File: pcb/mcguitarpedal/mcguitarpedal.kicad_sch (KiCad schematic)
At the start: 74 parts, among them J1 IN, J10 ENCODER2, J11 ENCODER3, J2 PREAMP_HEADERS, J3 BTN_MTX, J4 OUT, J5 EXP, J6 ILI9488 Module, J7 PWR_IN, J8 POT_HP_VOLUME_10k, J9 ENCODER1, Q1 2N3904, Q2 BC416, SW1 SW_BYPASS, SW2 SW_TUNER, SW3 SW_PRESET, SW5 SW_PWR, U1 Teensy4.1, U2 Teensy Audio Board, U4 74HC148, U6 STPDWN-3P-5V, U7 STDN-3A24-ADJ, U8 74HCT595D

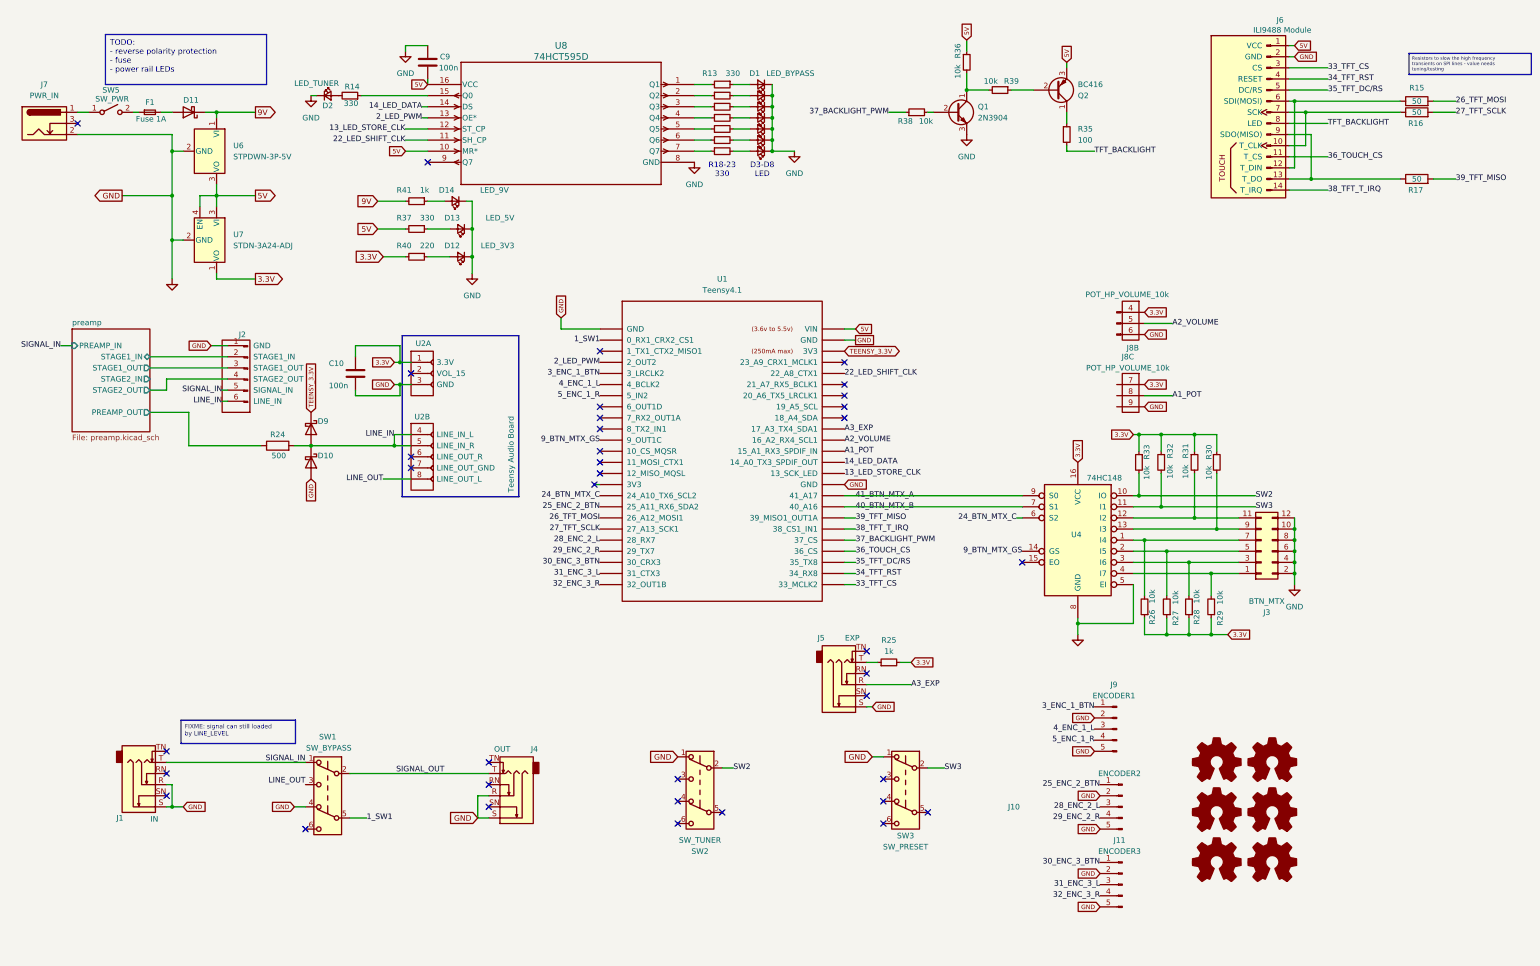
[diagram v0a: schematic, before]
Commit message: Silkscreen labeling
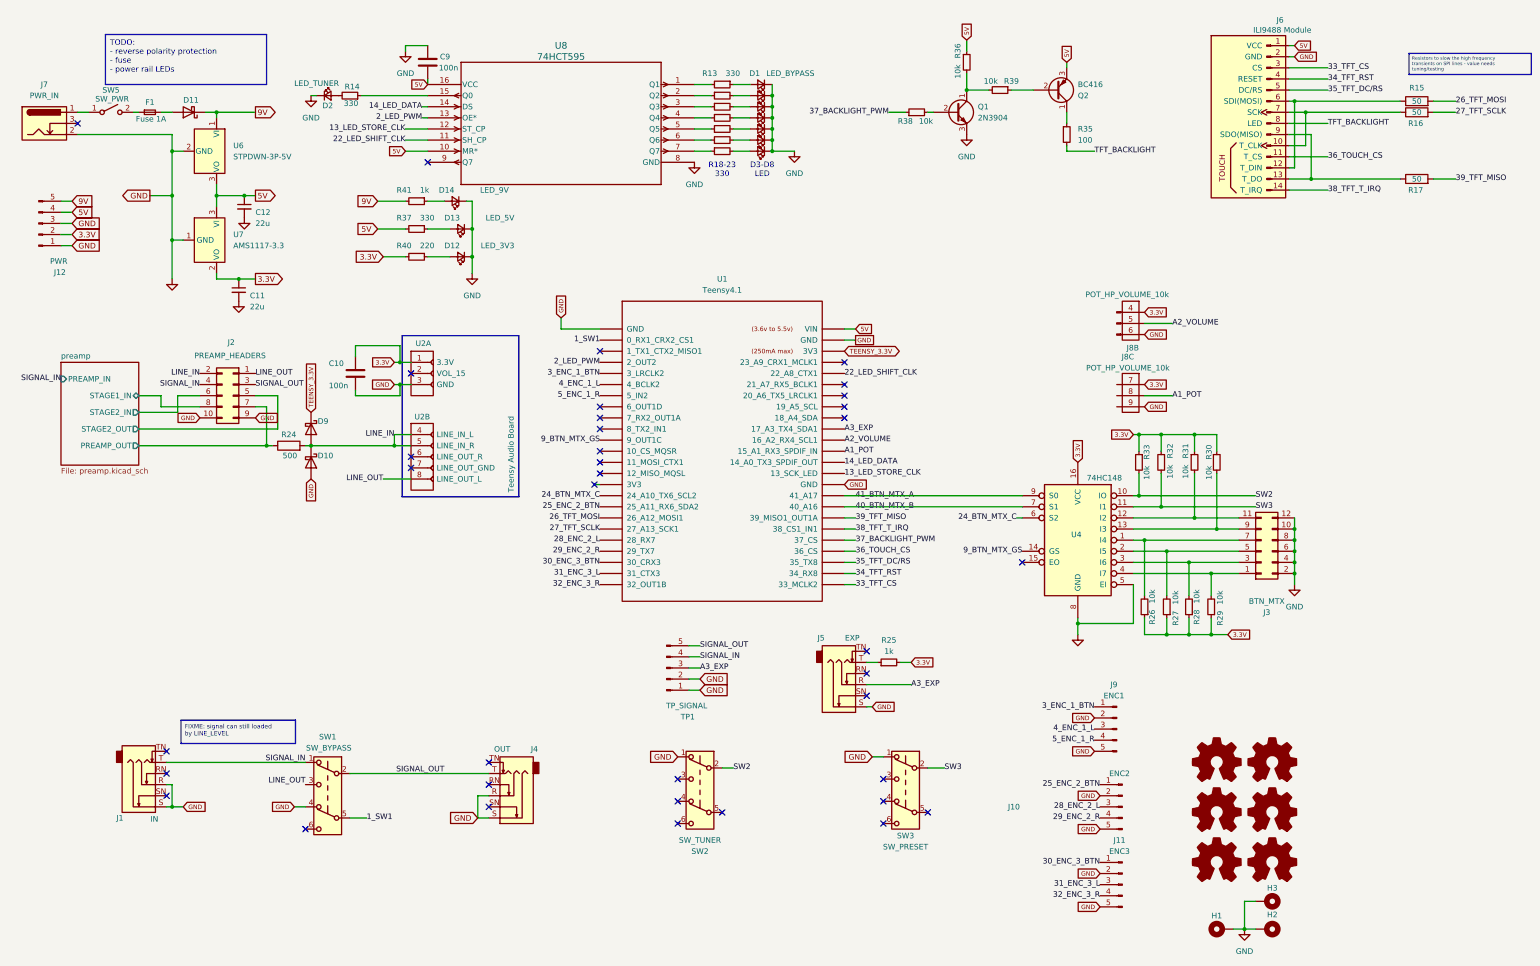
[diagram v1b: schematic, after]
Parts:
- removed U7: STDN-3A24-ADJ, mcguitarpedal:STPDN-3A24-ADJ, symbol mcguitarpedal:STDN-3A24-ADJ
- added C11, C12: 22u, Capacitor_Tantalum_SMD:CP_EIA-7343-30_AVX-N_Pad2.25x2.55mm_HandSolder, symbol Device:C_Small
- added H1, H2, H3: MountingHole_Pad, MountingHole:MountingHole_2.2mm_M2_Pad, symbol Mechanical:MountingHole_Pad
- added J12: PWR, Connector_PinHeader_2.54mm:PinHeader_1x05_P2.54mm_Vertical, symbol Connector:Conn_01x05_Pin
- added TP1: TP_SIGNAL, Connector_PinHeader_2.54mm:PinHeader_1x05_P2.54mm_Vertical, symbol Connector:Conn_01x05_Pin
- added U7: AMS1117-3.3, Package_TO_SOT_SMD:SOT-223-3_TabPin2, symbol Regulator_Linear:AMS1117-3.3
- C9: footprint Capacitor_THT:C_Rect_L7.2mm_W2.5mm_P5.00mm_FKS2_FKP2_MKS2_MKP2 -> Capacitor_SMD:C_1206_3216Metric_Pad1.33x1.80mm_HandSolder
- J10: value ENCODER2 -> ENC2; footprint Connector_PinHeader_2.54mm:PinHeader_1x05_P2.54mm_Vertical -> mcguitarpedal:Encoder_headers
- J11: value ENCODER3 -> ENC3; footprint Connector_PinHeader_2.54mm:PinHeader_1x05_P2.54mm_Vertical -> mcguitarpedal:Encoder_headers
- J2: footprint Connector_PinHeader_2.54mm:PinHeader_1x06_P2.54mm_Vertical -> mcguitarpedal:PREAMP_HEADERS; symbol mcguitarpedal:Preamp_headers -> Connector_Generic:Conn_02x05_Odd_Even
- J9: value ENCODER1 -> ENC1; footprint Connector_PinHeader_2.54mm:PinHeader_1x05_P2.54mm_Vertical -> mcguitarpedal:Encoder_headers
- U8: value 74HCT595D -> 74HCT595
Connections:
- net preamp/STAGE1_OUT is gone; now on net SIGNAL_OUT: J2.3 (Pin_3)
- net 3.3V: now also C11.1, J12.2 (Pin_2), U7.2 (VO)
- net 5V: now also C12.1, J12.4 (Pin_4), U7.3 (VI)
- net 9V: now also J12.5 (Pin_5)
- net A3_EXP: now also TP1.3 (Pin_3)
- net GND: now also J2.10 (Pin_10), J2.9 (Pin_9), C11.2, C12.2, H1.1, H2.1, H3.1, J12.1 (Pin_1), J12.3 (Pin_3), TP1.1 (Pin_1), TP1.2 (Pin_2), U7.1 (GND); no longer J2.1 (GND)
- net LINE_IN: now also J2.2 (Pin_2); no longer J2.6 (LINE_IN)
- net LINE_OUT: now also J2.1 (Pin_1)
- net SIGNAL_IN: now also J2.4 (Pin_4), TP1.4 (Pin_4); no longer J2.5 (SIGNAL_IN)
- net SIGNAL_OUT: now also TP1.5 (Pin_5)
- net preamp/PREAMP_OUT: now also J2.7 (Pin_7)
- net preamp/STAGE1_IN: now also J2.8 (Pin_8); no longer J2.2 (STAGE1_IN)
- net preamp/STAGE2_IN: now also J2.6 (Pin_6)
- net preamp/STAGE2_OUT: now also J2.5 (Pin_5); no longer J2.4 (STAGE2_OUT)
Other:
- sheet preamp ports: added none; removed STAGE1_OUT
- moved on the sheet: R24

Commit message: Final 1.0 design
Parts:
- added C1, C6: 22u, Capacitor_Tantalum_SMD:CP_EIA-3216-18_Kemet-A_Pad1.58x1.35mm_HandSolder, symbol Device:C_Small
- added C2, C4, C9: 100n, Capacitor_SMD:C_1206_3216Metric_Pad1.33x1.80mm_HandSolder, symbol Device:C_Small
- added H1: MountingHole_Pad, MountingHole:MountingHole_2.2mm_M2_Pad, symbol Mechanical:MountingHole_Pad
- added R20: 10k, Resistor_SMD:R_1206_3216Metric_Pad1.30x1.75mm_HandSolder, symbol Device:R_Small
- added TP2: SHIFT_CLK, TestPoint:TestPoint_Loop_D1.80mm_Drill1.0mm_Beaded, symbol Connector:TestPoint
- added TP3: TP_LED_DATA, TestPoint:TestPoint_Loop_D1.80mm_Drill1.0mm_Beaded, symbol Connector:TestPoint
- added TP4: TP_STORE_CLK, TestPoint:TestPoint_Loop_D1.80mm_Drill1.0mm_Beaded, symbol Connector:TestPoint
- added TP5: TP_MOSI, TestPoint:TestPoint_Loop_D1.80mm_Drill1.0mm_Beaded, symbol Connector:TestPoint
- added TP6: TP_SCLK, TestPoint:TestPoint_Loop_D1.80mm_Drill1.0mm_Beaded, symbol Connector:TestPoint
- added TP7: TP_MISO, TestPoint:TestPoint_Loop_D1.80mm_Drill1.0mm_Beaded, symbol Connector:TestPoint
- C3: renamed from C11; footprint Capacitor_Tantalum_SMD:CP_EIA-7343-30_AVX-N_Pad2.25x2.55mm_HandSolder -> Capacitor_Tantalum_SMD:CP_EIA-3216-18_Kemet-A_Pad1.58x1.35mm_HandSolder
- C5: renamed from C12; footprint Capacitor_Tantalum_SMD:CP_EIA-7343-30_AVX-N_Pad2.25x2.55mm_HandSolder -> Capacitor_Tantalum_SMD:CP_EIA-3216-18_Kemet-A_Pad1.58x1.35mm_HandSolder
- C7: renamed from C10; symbol Device:C -> Device:C_Small
- R16: renamed from R25; value 1k -> 330; footprint Resistor_THT:R_Axial_DIN0207_L6.3mm_D2.5mm_P7.62mm_Horizontal -> Resistor_SMD:R_1206_3216Metric_Pad1.30x1.75mm_HandSolder
- renumbered C9 to C8, D11 to D1, D7 to D10, D6 to D11, D5 to D12, D4 to D13, D3 to D14, D9 to D2, D10 to D3, D2 to D4, D14 to D5, D13 to D6, D12 to D7, D1 to D8, D8 to D9, H1 to H2, H2 to H4, J4 to J1, J3 to J12, J5 to J2, J1 to J3, J12 to J4, J7 to J5, J2 to J6, J6 to J7, R24 to R1, R20 to R10, R19 to R11, R18 to R12, R38 to R13, R36 to R14, R39 to R15, R35 to R17, R33 to R18, R26 to R19, R14 to R2, R32 to R21, R27 to R22, R28 to R23, R31 to R24, R29 to R25, R30 to R26, R15 to R27, R16 to R28, R17 to R29, R41 to R3, R37 to R4, R40 to R5, R13 to R6, R23 to R7, R22 to R8, R21 to R9, SW5 to SW1, SW1 to SW2, SW2 to SW3, SW3 to SW4, U6 to U4, U7 to U5, U8 to U6, U4 to U7
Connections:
- net 13_LED_STORE_CLK: now also TP4.1
- net 14_LED_DATA: now also TP3.1
- net 22_LED_SHIFT_CLK: now also TP2.1
- net 3.3V: now also C6.1, C9.1, R20.2
- net 36_TOUCH_CS: now also R20.1
- net 39_TFT_MISO: now also TP7.1
- net 5V: now also C1.2, C2.1
- net 9V: now also C4.1
- net GND: now also C1.1, C2.2, C4.2, C6.2, C9.2, H1.1
- net at J7.12 (T_DIN), J7.6 (SDI(MOSI)), R27.1: now also TP5.1
- net at J7.10 (T_CLK), J7.7 (SCK), R28.1: now also TP6.1
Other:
- moved on the sheet: C3, D5, D6, D7, J7, Q1, Q2, R13, R14, R15, R17, R27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

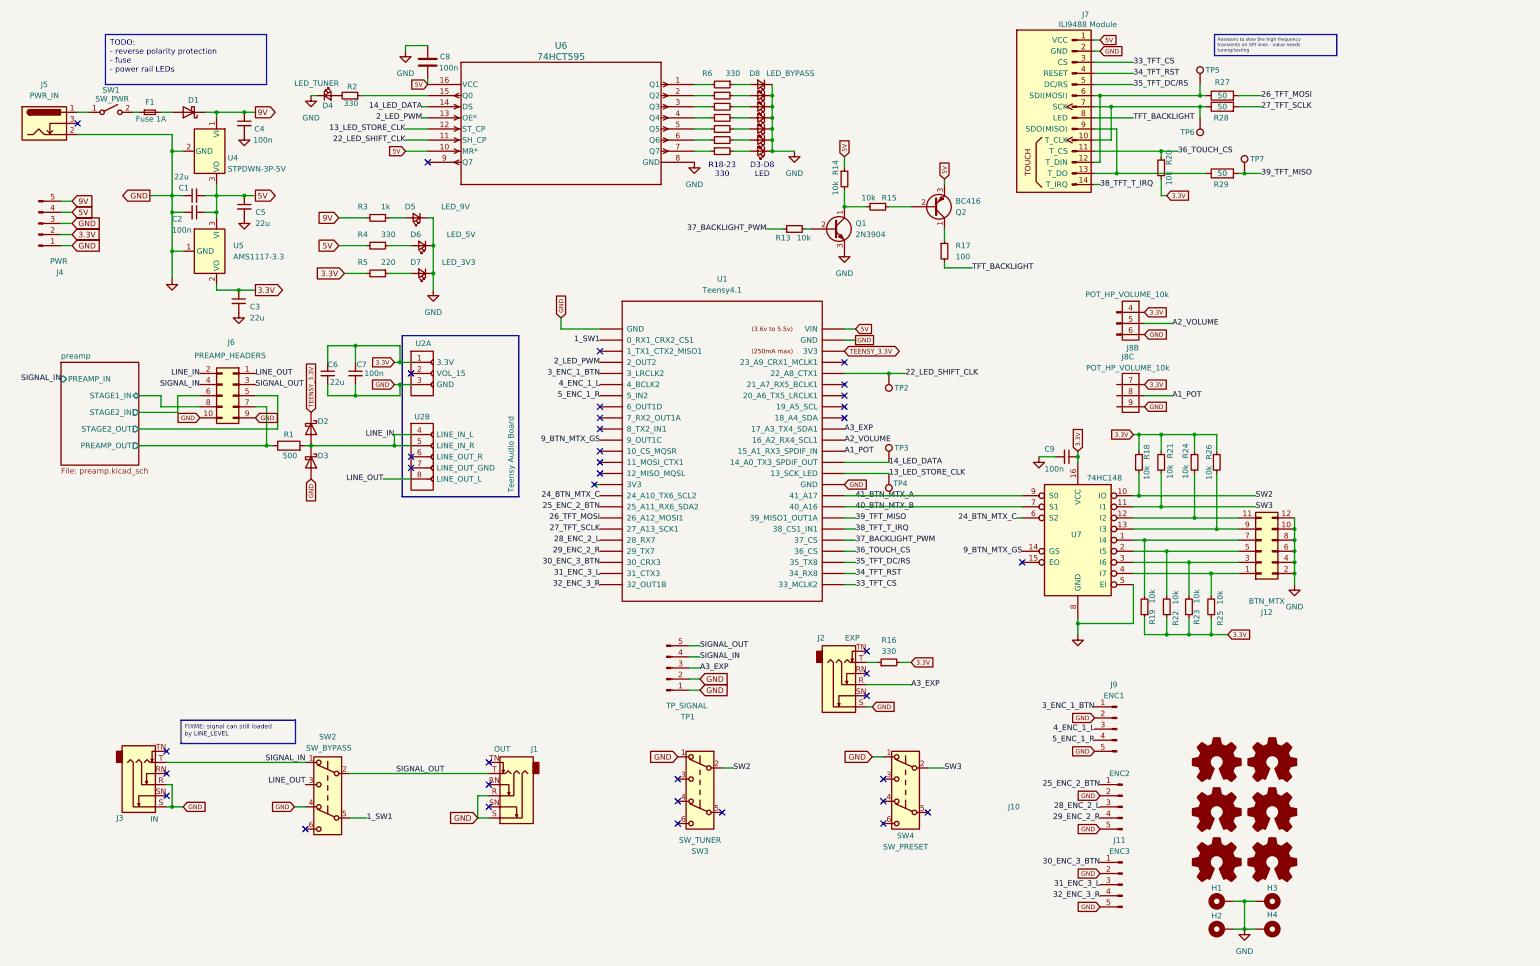
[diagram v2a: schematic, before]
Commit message: Missing models, PCB pdf exports
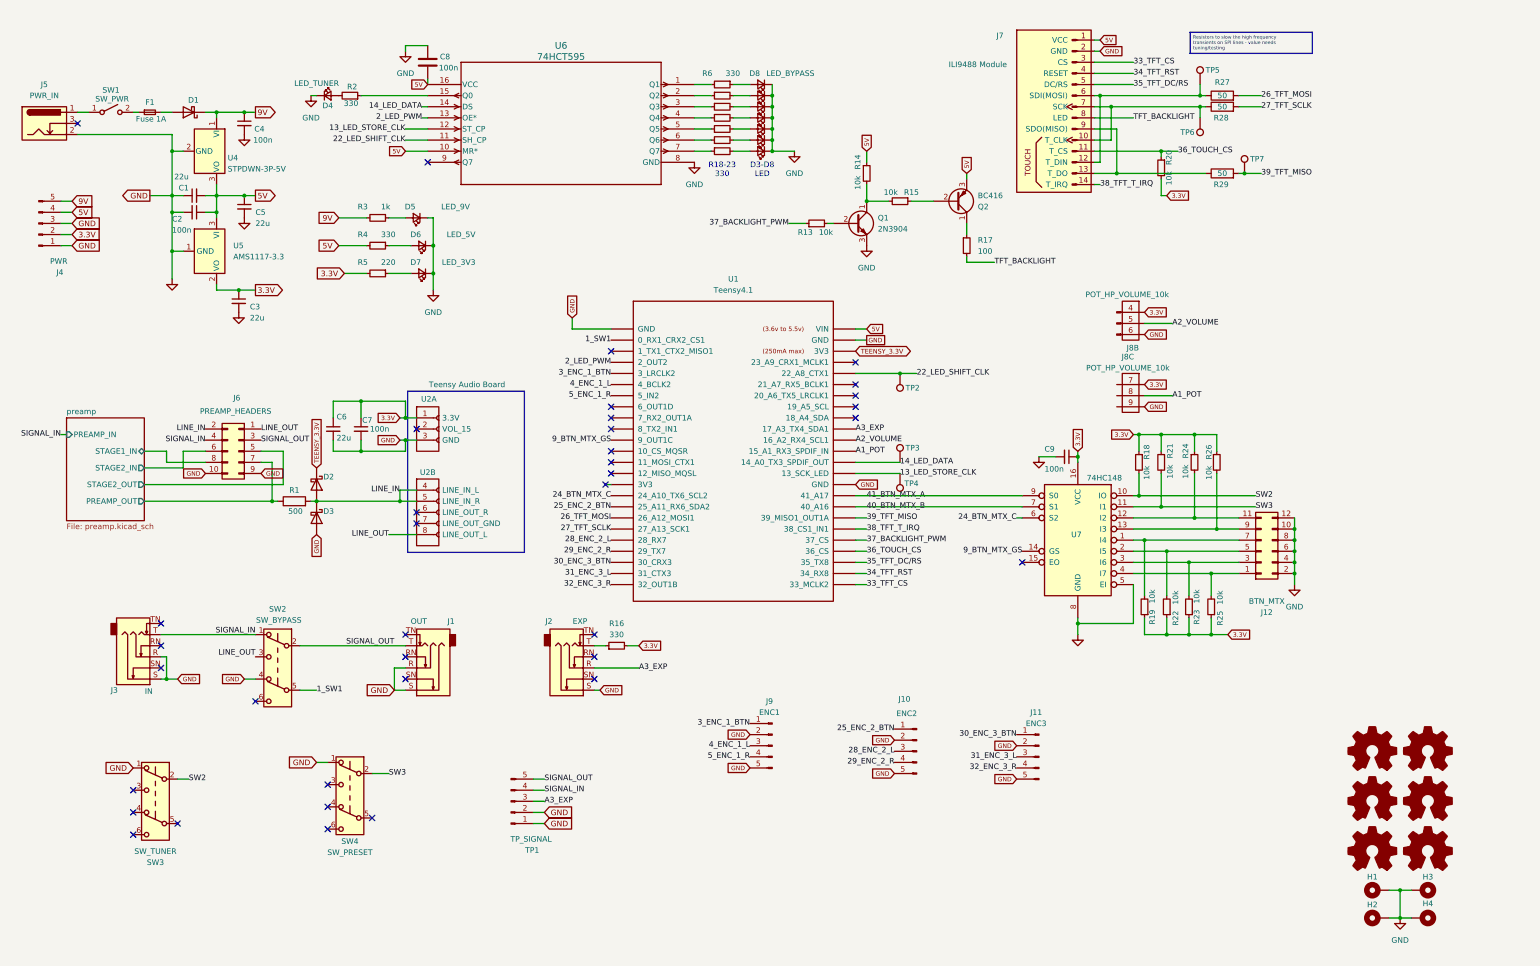
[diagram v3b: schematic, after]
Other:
- moved on the sheet: C6, C7, D2, D3, H1, H2, H3, H4, J1, J10, J11, J2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
